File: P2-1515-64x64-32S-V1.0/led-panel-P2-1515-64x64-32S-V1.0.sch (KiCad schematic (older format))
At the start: 67 parts, among them T1 SM5166P, T2 SM5166P, T3 SM5166P, T4 SM5166P, T5 SM5166P, T6 SM5166P, T7 SM5166P, T8 SM5166P, U1 DP74HC245, U2 DP74HC245, U4 SM74HC04

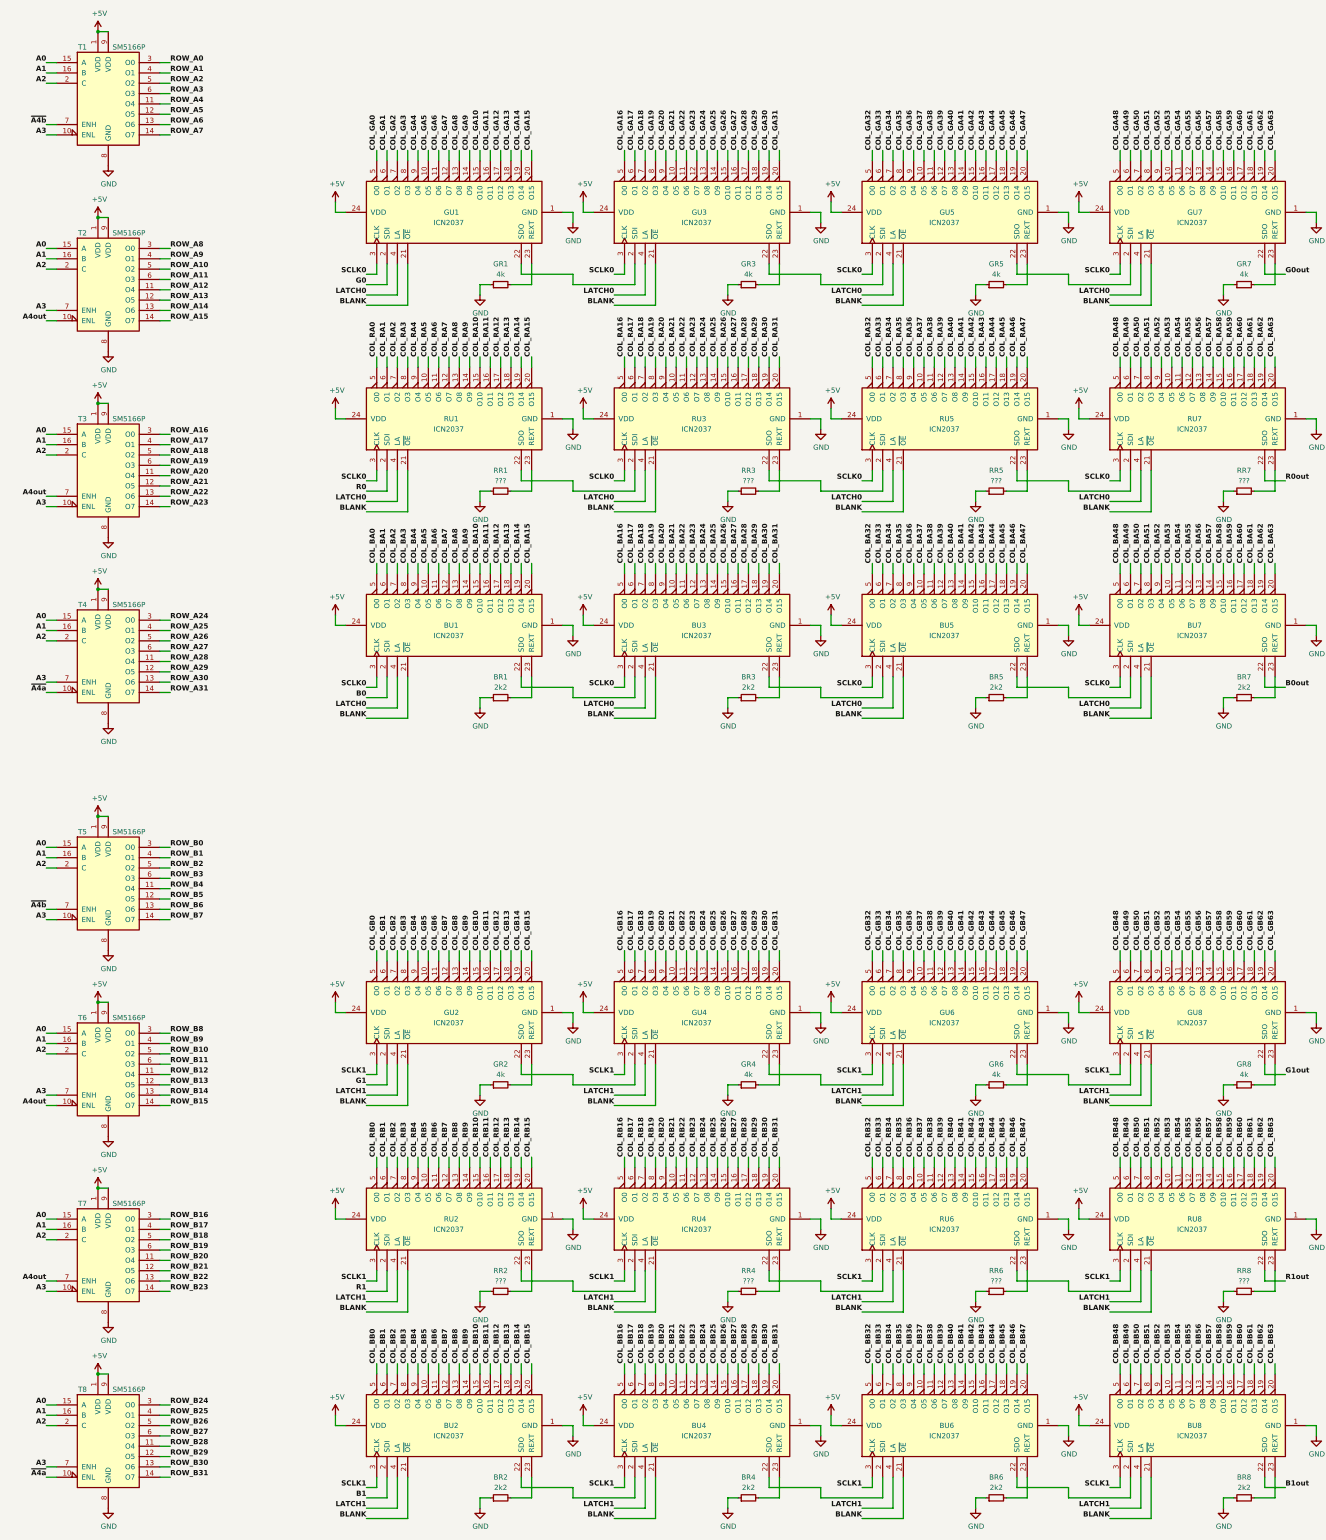
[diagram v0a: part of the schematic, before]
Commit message: Corrected some reference IDs.
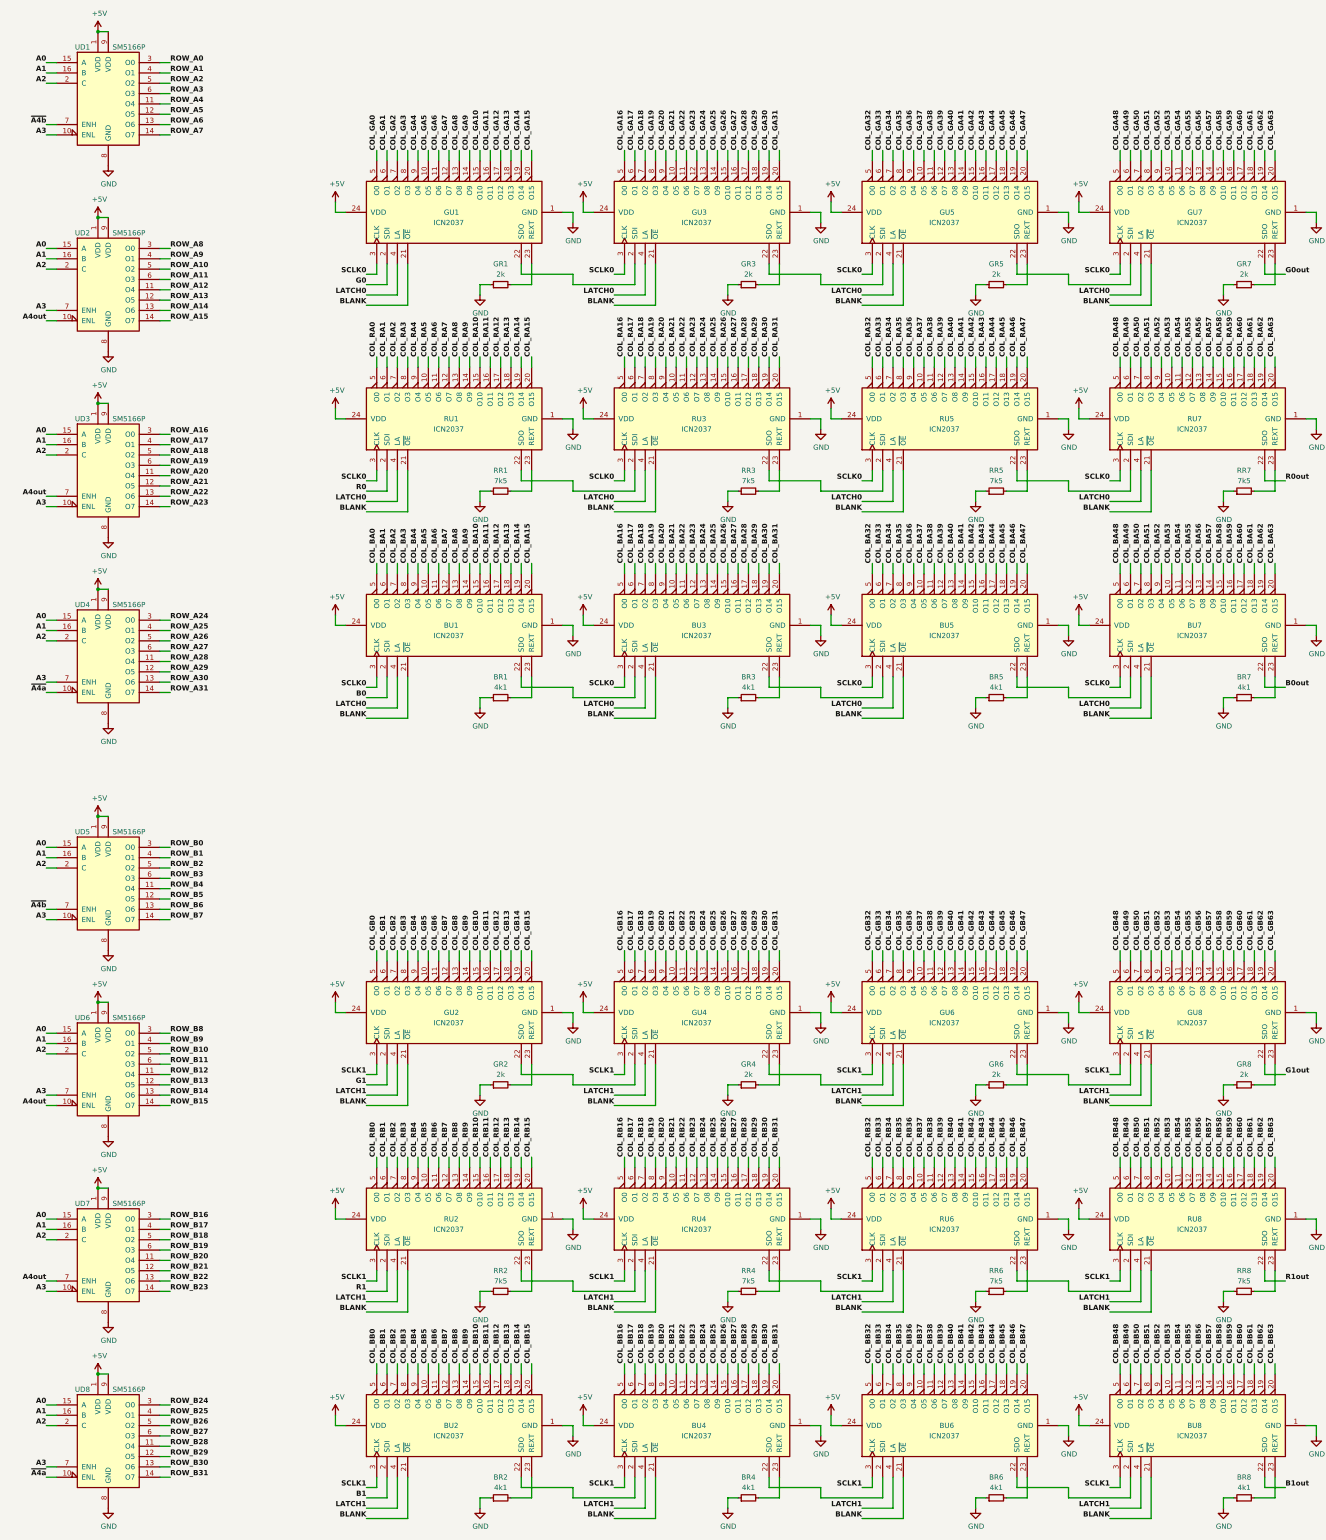
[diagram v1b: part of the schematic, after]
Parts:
- BR1, BR2, BR3, BR4, BR5, BR6, BR7, BR8: value 2k2 -> 4k1
- GR1, GR2, GR3, GR4, GR5, GR6, GR7, GR8: value 4k -> 2k
- RR1, RR2, RR3, RR4, RR5, RR6, RR7, RR8: value ??? -> 7k5
- renumbered T1 to UD1, T2 to UD2, T3 to UD3, T4 to UD4, T5 to UD5, T6 to UD6, T7 to UD7, T8 to UD8
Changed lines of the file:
@@
 P 8100 3250
 F 0 "GR1" V 8300 3250 50  0000 C CNN
-F 1 "4k" V 8200 3250 50  0000 C CNN
+F 1 "2k" V 8200 3250 50  0000 C CNN
 F 2 "" H 8100 3250 50  0001 C CNN
 F 3 "~" H 8100 3250 50  0001 C CNN
@@
 P 10500 3250
 F 0 "GR3" V 10700 3250 50  0000 C CNN
-F 1 "4k" V 10600 3250 50  0000 C CNN
+F 1 "2k" V 10600 3250 50  0000 C CNN
 F 2 "" H 10500 3250 50  0001 C CNN
 F 3 "~" H 10500 3250 50  0001 C CNN
@@
 P 12900 3250
 F 0 "GR5" V 13100 3250 50  0000 C CNN
-F 1 "4k" V 13000 3250 50  0000 C CNN
+F 1 "2k" V 13000 3250 50  0000 C CNN
 F 2 "" H 12900 3250 50  0001 C CNN
 F 3 "~" H 12900 3250 50  0001 C CNN
@@
 P 15300 3250
 F 0 "GR7" V 15500 3250 50  0000 C CNN
-F 1 "4k" V 15400 3250 50  0000 C CNN
+F 1 "2k" V 15400 3250 50  0000 C CNN
 F 2 "" H 15300 3250 50  0001 C CNN
 F 3 "~" H 15300 3250 50  0001 C CNN
@@
 P 8100 5250
 F 0 "RR1" V 8300 5250 50  0000 C CNN
-F 1 "???" V 8200 5250 50  0000 C CNN
+F 1 "7k5" V 8200 5250 50  0000 C CNN
 F 2 "" H 8100 5250 50  0001 C CNN
 F 3 "~" H 8100 5250 50  0001 C CNN
@@
 P 10500 5250
 F 0 "RR3" V 10700 5250 50  0000 C CNN
-F 1 "???" V 10600 5250 50  0000 C CNN
+F 1 "7k5" V 10600 5250 50  0000 C CNN
 F 2 "" H 10500 5250 50  0001 C CNN
 F 3 "~" H 10500 5250 50  0001 C CNN
@@
 P 12900 5250
 F 0 "RR5" V 13100 5250 50  0000 C CNN
-F 1 "???" V 13000 5250 50  0000 C CNN
+F 1 "7k5" V 13000 5250 50  0000 C CNN
 F 2 "" H 12900 5250 50  0001 C CNN
 F 3 "~" H 12900 5250 50  0001 C CNN
@@
 P 15300 5250
 F 0 "RR7" V 15500 5250 50  0000 C CNN
-F 1 "???" V 15400 5250 50  0000 C CNN
+F 1 "7k5" V 15400 5250 50  0000 C CNN
 F 2 "" H 15300 5250 50  0001 C CNN
 F 3 "~" H 15300 5250 50  0001 C CNN
@@
 P 8100 7250
 F 0 "BR1" V 8300 7250 50  0000 C CNN
-F 1 "2k2" V 8200 7250 50  0000 C CNN
+F 1 "4k1" V 8200 7250 50  0000 C CNN
 F 2 "" H 8100 7250 50  0001 C CNN
 F 3 "~" H 8100 7250 50  0001 C CNN
@@
 P 10500 7250
 F 0 "BR3" V 10700 7250 50  0000 C CNN
-F 1 "2k2" V 10600 7250 50  0000 C CNN
+F 1 "4k1" V 10600 7250 50  0000 C CNN
 F 2 "" H 10500 7250 50  0001 C CNN
 F 3 "~" H 10500 7250 50  0001 C CNN
@@
 P 12900 7250
 F 0 "BR5" V 13100 7250 50  0000 C CNN
-F 1 "2k2" V 13000 7250 50  0000 C CNN
+F 1 "4k1" V 13000 7250 50  0000 C CNN
 F 2 "" H 12900 7250 50  0001 C CNN
 F 3 "~" H 12900 7250 50  0001 C CNN
@@
 P 15300 7250
 F 0 "BR7" V 15500 7250 50  0000 C CNN
-F 1 "2k2" V 15400 7250 50  0000 C CNN
+F 1 "4k1" V 15400 7250 50  0000 C CNN
 F 2 "" H 15300 7250 50  0001 C CNN
 F 3 "~" H 15300 7250 50  0001 C CNN
@@
 P 8100 11000
 F 0 "GR2" V 8300 11000 50  0000 C CNN
-F 1 "4k" V 8200 11000 50  0000 C CNN
+F 1 "2k" V 8200 11000 50  0000 C CNN
 F 2 "" H 8100 11000 50  0001 C CNN
 F 3 "~" H 8100 11000 50  0001 C CNN
@@
 P 10500 11000
 F 0 "GR4" V 10700 11000 50  0000 C CNN
-F 1 "4k" V 10600 11000 50  0000 C CNN
+F 1 "2k" V 10600 11000 50  0000 C CNN
 F 2 "" H 10500 11000 50  0001 C CNN
 F 3 "~" H 10500 11000 50  0001 C CNN
@@
 P 12900 11000
 F 0 "GR6" V 13100 11000 50  0000 C CNN
-F 1 "4k" V 13000 11000 50  0000 C CNN
+F 1 "2k" V 13000 11000 50  0000 C CNN
 F 2 "" H 12900 11000 50  0001 C CNN
 F 3 "~" H 12900 11000 50  0001 C CNN
@@
 P 15300 11000
 F 0 "GR8" V 15500 11000 50  0000 C CNN
-F 1 "4k" V 15400 11000 50  0000 C CNN
+F 1 "2k" V 15400 11000 50  0000 C CNN
 F 2 "" H 15300 11000 50  0001 C CNN
 F 3 "~" H 15300 11000 50  0001 C CNN
@@
 P 8100 13000
 F 0 "RR2" V 8300 13000 50  0000 C CNN
-F 1 "???" V 8200 13000 50  0000 C CNN
+F 1 "7k5" V 8200 13000 50  0000 C CNN
 F 2 "" H 8100 13000 50  0001 C CNN
 F 3 "~" H 8100 13000 50  0001 C CNN
@@
 P 10500 13000
 F 0 "RR4" V 10700 13000 50  0000 C CNN
-F 1 "???" V 10600 13000 50  0000 C CNN
+F 1 "7k5" V 10600 13000 50  0000 C CNN
 F 2 "" H 10500 13000 50  0001 C CNN
 F 3 "~" H 10500 13000 50  0001 C CNN
@@
 P 12900 13000
 F 0 "RR6" V 13100 13000 50  0000 C CNN
-F 1 "???" V 13000 13000 50  0000 C CNN
+F 1 "7k5" V 13000 13000 50  0000 C CNN
 F 2 "" H 12900 13000 50  0001 C CNN
 F 3 "~" H 12900 13000 50  0001 C CNN
@@
 P 15300 13000
 F 0 "RR8" V 15500 13000 50  0000 C CNN
-F 1 "???" V 15400 13000 50  0000 C CNN
+F 1 "7k5" V 15400 13000 50  0000 C CNN
 F 2 "" H 15300 13000 50  0001 C CNN
 F 3 "~" H 15300 13000 50  0001 C CNN
@@
 P 8100 15000
 F 0 "BR2" V 8300 15000 50  0000 C CNN
-F 1 "2k2" V 8200 15000 50  0000 C CNN
+F 1 "4k1" V 8200 15000 50  0000 C CNN
 F 2 "" H 8100 15000 50  0001 C CNN
 F 3 "~" H 8100 15000 50  0001 C CNN
@@
 P 10500 15000
 F 0 "BR4" V 10700 15000 50  0000 C CNN
-F 1 "2k2" V 10600 15000 50  0000 C CNN
+F 1 "4k1" V 10600 15000 50  0000 C CNN
 F 2 "" H 10500 15000 50  0001 C CNN
 F 3 "~" H 10500 15000 50  0001 C CNN
@@
 P 12900 15000
 F 0 "BR6" V 13100 15000 50  0000 C CNN
-F 1 "2k2" V 13000 15000 50  0000 C CNN
+F 1 "4k1" V 13000 15000 50  0000 C CNN
 F 2 "" H 12900 15000 50  0001 C CNN
 F 3 "~" H 12900 15000 50  0001 C CNN
@@
 P 15300 15000
 F 0 "BR8" V 15500 15000 50  0000 C CNN
-F 1 "2k2" V 15400 15000 50  0000 C CNN
+F 1 "4k1" V 15400 15000 50  0000 C CNN
 F 2 "" H 15300 15000 50  0001 C CNN
 F 3 "~" H 15300 15000 50  0001 C CNN
@@
 	3800 5400 3700 5400
 $Comp
-L led-panel-chipset:TC7258E T4
+L led-panel-chipset:TC7258E UD4
 U 1 1 5CEDF3F6
 P 4300 6800
-F 0 "T4" H 4050 7250 50  0000 C CNN
+F 0 "UD4" H 4050 7250 50  0000 C CNN
 F 1 "SM5166P" H 4500 7250 50  0000 C CNN
 F 2 "" H 4300 7800 50  0001 C CNN
@@
 	3800 7200 3700 7200
 $Comp
-L led-panel-chipset:TC7258E T5
+L led-panel-chipset:TC7258E UD5
 U 1 1 5D0AF692
 P 4300 9000
-F 0 "T5" H 4050 9450 50  0000 C CNN
+F 0 "UD5" H 4050 9450 50  0000 C CNN
 F 1 "SM5166P" H 4500 9450 50  0000 C CNN
 F 2 "" H 4300 10000 50  0001 C CNN
@@
 	3800 9400 3700 9400
 $Comp
-L led-panel-chipset:TC7258E T6
+L led-panel-chipset:TC7258E UD6
 U 1 1 5D0AF6B4
 P 4300 10800
-F 0 "T6" H 4050 11250 50  0000 C CNN
+F 0 "UD6" H 4050 11250 50  0000 C CNN
 F 1 "SM5166P" H 4500 11250 50  0000 C CNN
 F 2 "" H 4300 11800 50  0001 C CNN
@@
 	3800 11200 3700 11200
 $Comp
-L led-panel-chipset:TC7258E T7
+L led-panel-chipset:TC7258E UD7
 U 1 1 5D0AF6D5
 P 4300 12600
-F 0 "T7" H 4050 13050 50  0000 C CNN
+F 0 "UD7" H 4050 13050 50  0000 C CNN
 F 1 "SM5166P" H 4500 13050 50  0000 C CNN
 F 2 "" H 4300 13600 50  0001 C CNN
@@
 	3800 13000 3700 13000
 $Comp
-L led-panel-chipset:TC7258E T8
+L led-panel-chipset:TC7258E UD8
 U 1 1 5D0AF6F6
 P 4300 14400
-F 0 "T8" H 4050 14850 50  0000 C CNN
+F 0 "UD8" H 4050 14850 50  0000 C CNN
 F 1 "SM5166P" H 4500 14850 50  0000 C CNN
 F 2 "" H 4300 15400 50  0001 C CNN
@@
 Connection ~ 4200 2600
 $Comp
-L led-panel-chipset:TC7258E T2
+L led-panel-chipset:TC7258E UD2
 U 1 1 5CCC7C4A
 P 4300 3200
-F 0 "T2" H 4050 3650 50  0000 C CNN
+F 0 "UD2" H 4050 3650 50  0000 C CNN
 F 1 "SM5166P" H 4500 3650 50  0000 C CNN
 F 2 "" H 4300 4200 50  0001 C CNN
@@
 Connection ~ 4200 800
 $Comp
-L led-panel-chipset:TC7258E T1
+L led-panel-chipset:TC7258E UD1
 U 1 1 5CAC5136
 P 4300 1400
-F 0 "T1" H 4050 1850 50  0000 C CNN
+F 0 "UD1" H 4050 1850 50  0000 C CNN
 F 1 "SM5166P" H 4500 1850 50  0000 C CNN
 F 2 "" H 4300 2400 50  0001 C CNN
@@
 Connection ~ 4200 4400
 $Comp
-L led-panel-chipset:TC7258E T3
+L led-panel-chipset:TC7258E UD3
 U 1 1 5CDD06E0
 P 4300 5000
-F 0 "T3" H 4050 5450 50  0000 C CNN
+F 0 "UD3" H 4050 5450 50  0000 C CNN
 F 1 "SM5166P" H 4500 5450 50  0000 C CNN
 F 2 "" H 4300 6000 50  0001 C CNN

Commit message: Corrected A4 net naming and routing.
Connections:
- net A4out is gone; now on net A4: UD2.10 (ENL), UD3.7 (ENH), UD6.10 (ENL), UD7.7 (ENH)
- net A4: now also U4.1; no longer U4.11, U4.13
- net GND: no longer U4.1, U4.3, U4.5, U4.9
- net ~A4: now reaches U4.2
- net ~A4: now also UD1.7 (ENH), UD4.10 (ENL), UD5.7 (ENH), UD8.10 (ENL)
- removed net ~A4a: U4.10, UD4.10 (ENL), UD8.10 (ENL)
- removed net ~A4b: U4.12, UD1.7 (ENH), UD5.7 (ENH)
- no-connect marks 4 -> 10
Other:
- moved on the sheet: U1, U1G, U2, U4E, U4F
